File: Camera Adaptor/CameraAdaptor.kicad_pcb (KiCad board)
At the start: 2 copper layers, 6 parts, among them P1 CONN_02X12, P2 CONN_02X09, U1 Oscillator

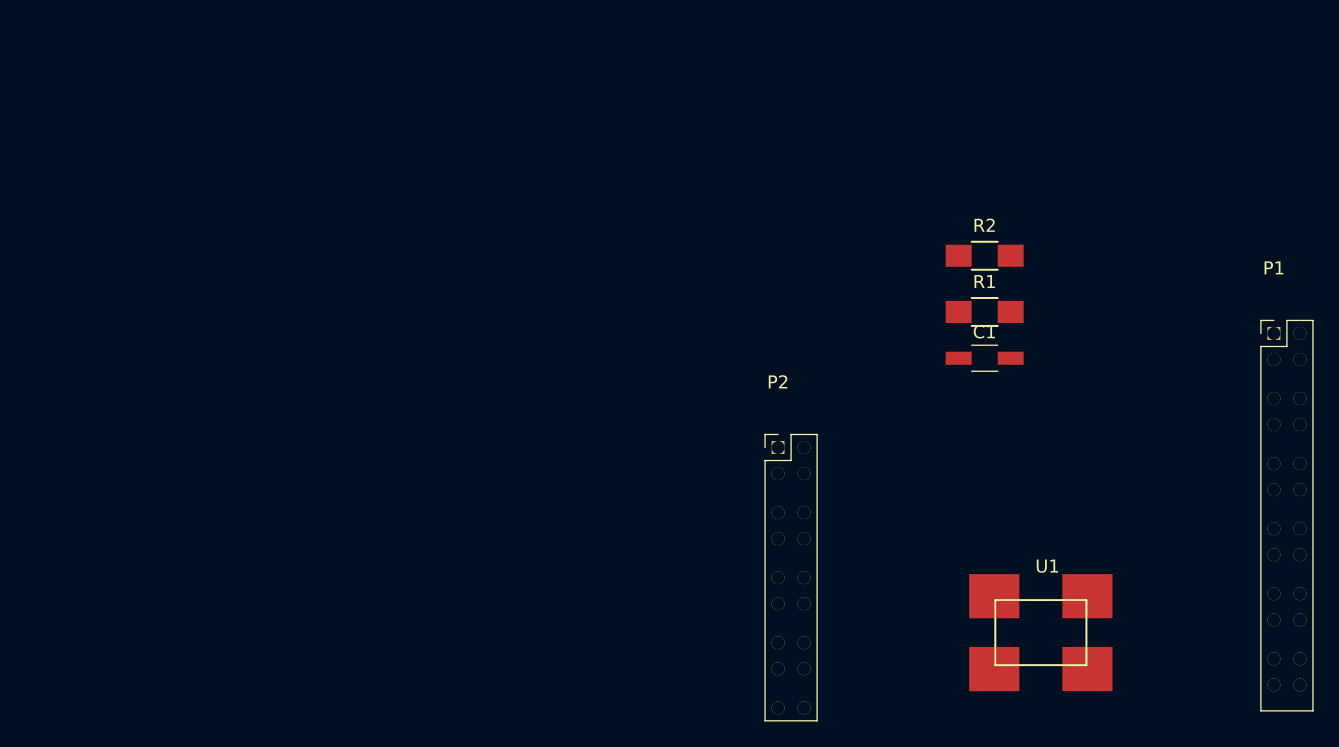
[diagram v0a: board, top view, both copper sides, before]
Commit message: Did the basic layout, avaiting via size, track width specifications.
Signed-off-by: Kolijn Wolfaardt <kolijn.wolfaardt@gmail.com>
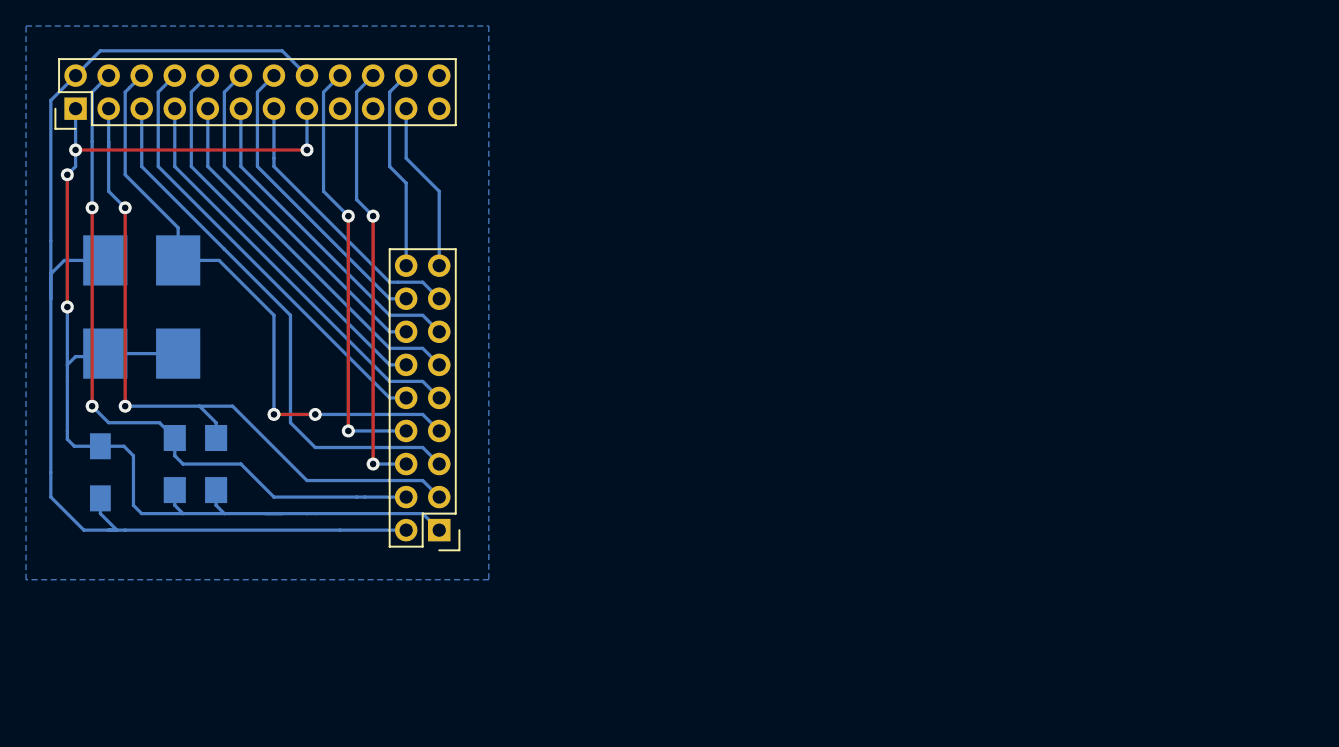
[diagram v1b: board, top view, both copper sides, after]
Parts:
- C1, R1, R2, U1: moved to B.Cu
- moved P1 93.7 mm to (81.9, 81.3), turned to 90 degrees
- moved U1 73.5 mm to (87.0, 96.5), turned to 90 degrees
- moved C1 68.5 mm to (83.8, 109.2), turned to 270 degrees
- moved R2 64.3 mm to (89.5, 108.6), turned to 90 degrees
- moved R1 60.2 mm to (92.7, 108.6), turned to 90 degrees
- moved P2 26.8 mm to (109.9, 113.7), turned to 180 degrees
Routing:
- net +3V3: track 0.00 -> 94.6 mm, vias 0 -> 4
- net GND: track 0.00 -> 91.0 mm
- net /SIOC: track 0.00 -> 54.0 mm, vias 0 -> 2
- net /SIOD: track 0.00 -> 53.7 mm, vias 0 -> 2
- net /PCLK: track 0.00 -> 46.4 mm, vias 0 -> 2
- net /VSync: track 0.00 -> 41.6 mm
- net /D6: track 0.00 -> 33.9 mm
- net /Href: track 0.00 -> 33.4 mm, vias 0 -> 2
- net /XCLK: track 0.00 -> 33.1 mm, vias 0 -> 2
- net /D7: track 0.00 -> 32.1 mm
- net /D4: track 0.00 -> 30.3 mm
- net /D5: track 0.00 -> 28.5 mm
- net /D2: track 0.00 -> 26.7 mm
- net /D3: track 0.00 -> 24.9 mm
- net /D0: track 0.00 -> 23.8 mm
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- added copper zone on B.Cu, net GND
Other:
- net class Default: via_dia 0.6 -> 1; via_drill 0.4 -> 0.8
- rule via_min_drill: 0.3 -> 0.6
- rule via_min_size: 0.4 -> 0.7

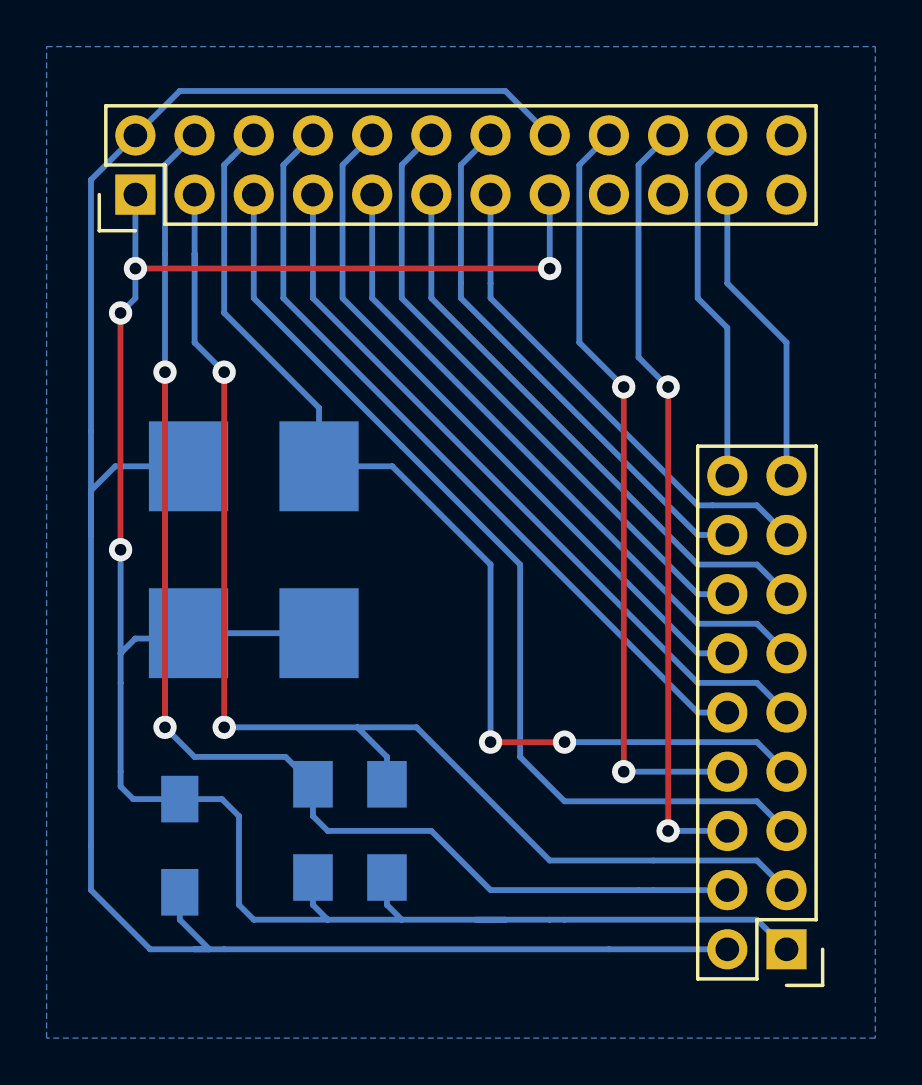
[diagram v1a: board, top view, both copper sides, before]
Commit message: Changed CamerAdaptor layout, changed track thickness
Signed-off-by: Kolijn Wolfaardt <kolijn.wolfaardt@gmail.com>
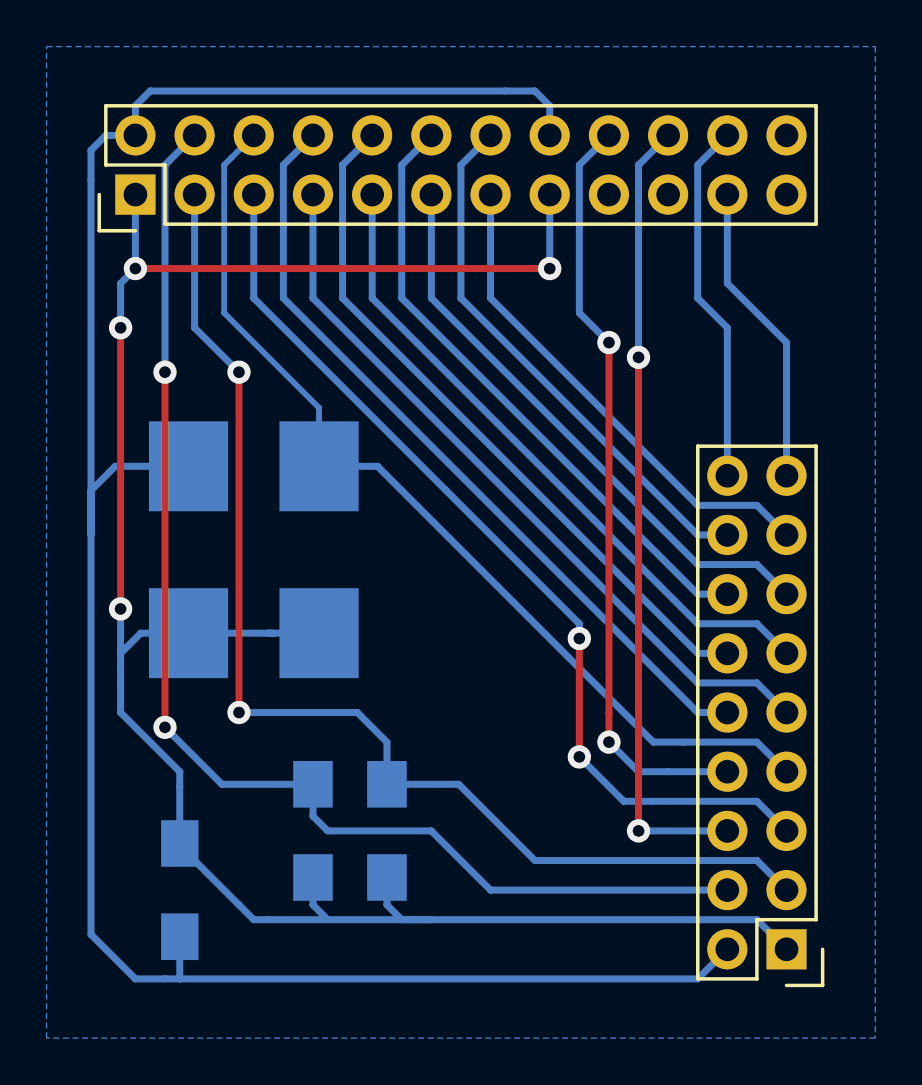
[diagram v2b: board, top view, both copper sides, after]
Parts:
- moved C1 1.91 mm to (83.8, 111.1)
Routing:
- net /PCLK: track 46.4 -> 41.9 mm, vias 2 -> 0
- net /SIOC: track 54.0 -> 50.7 mm
- net GND: track 91.0 -> 93.6 mm
- net /VSync: track 41.6 -> 40.1 mm, vias 0 -> 2
- net /Href: track 33.4 -> 34.2 mm
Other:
- net class Default: trace_width 0.25 -> 0.3
- rule via_min_drill: 0.6 -> 0.7
- rule via_min_size: 0.7 -> 0.8

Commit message: Removed pdf outputs, added correct gerber files
One of the gerber files doesn't register correct with
the cnc machine: The hole should be positioned at 80,100
but ends at 800,100

Signed-off-by: Kolijn Wolfaardt <kolijn.wolfaardt@gmail.com>
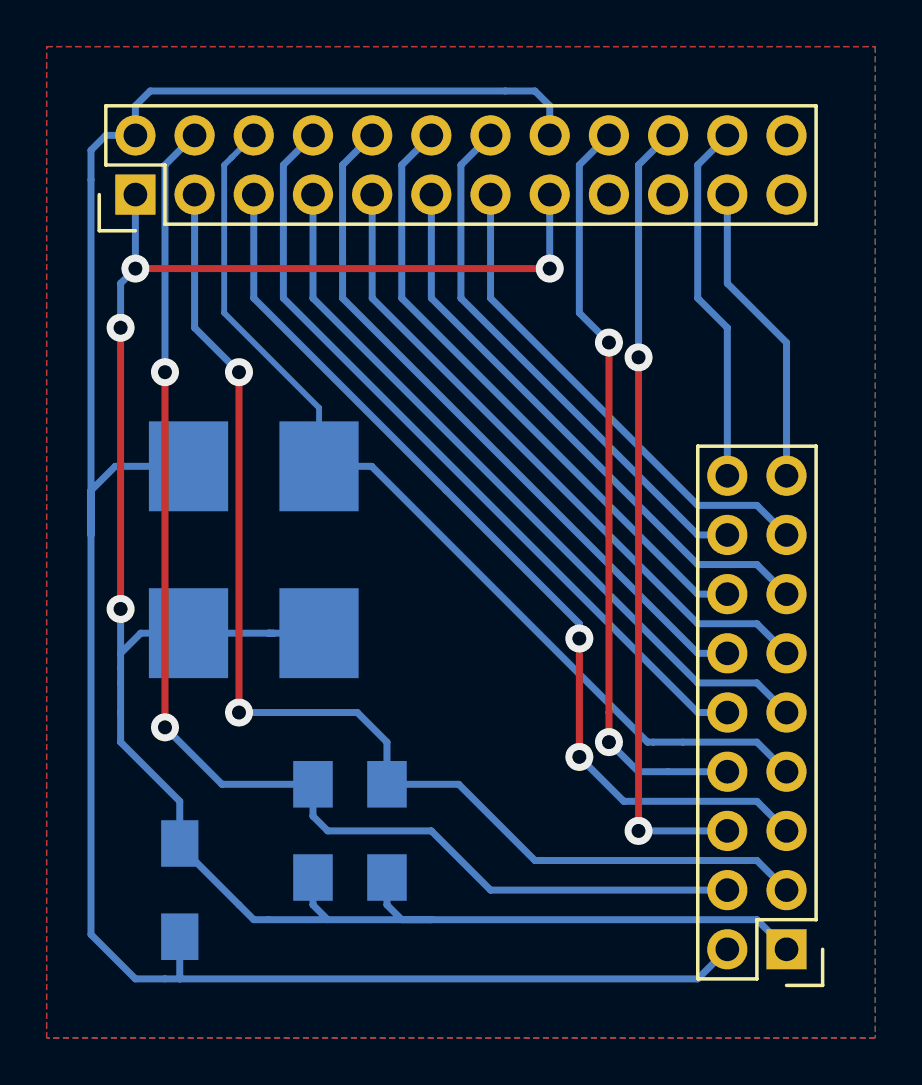
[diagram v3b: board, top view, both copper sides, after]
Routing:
- added copper zone on F.Cu, net GND
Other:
- net class Default: via_dia 1 -> 1.2

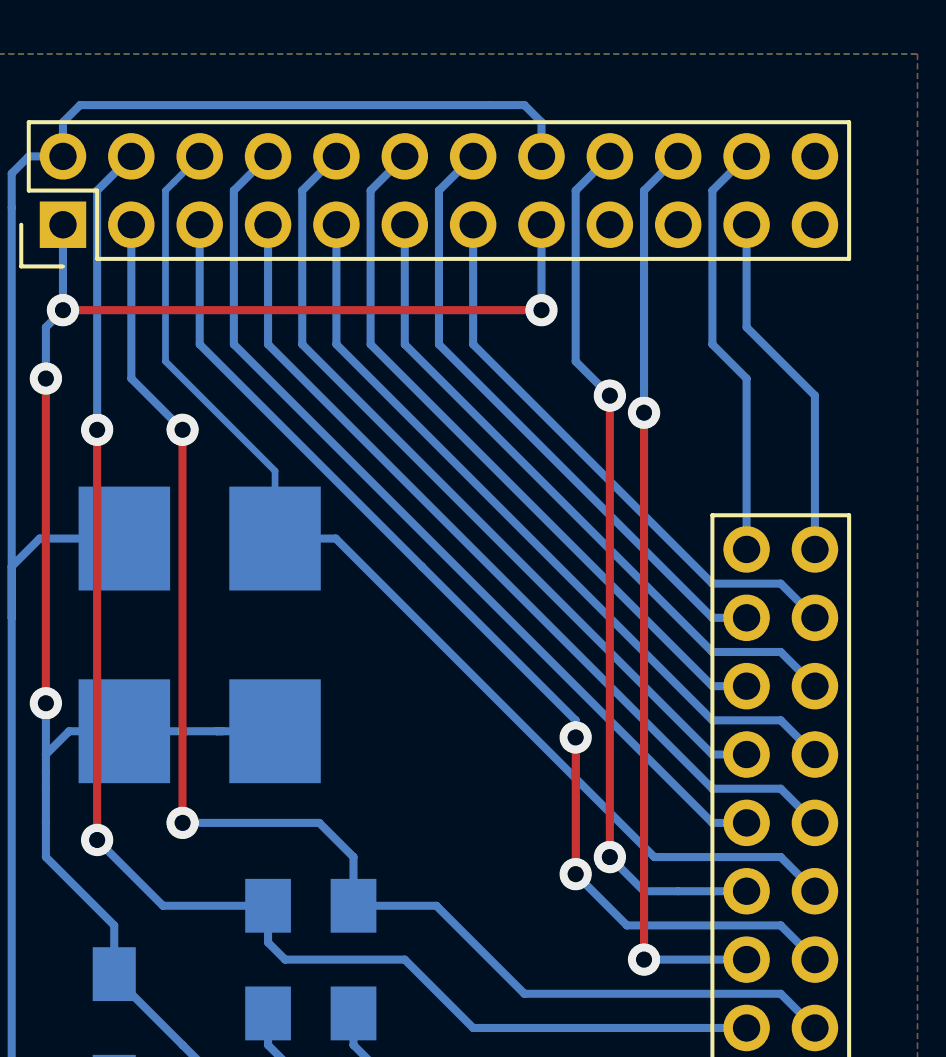
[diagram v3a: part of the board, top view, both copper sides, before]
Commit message: Fixed camera board
Signed-off-by: Kolijn Wolfaardt <kolijn.wolfaardt@gmail.com>
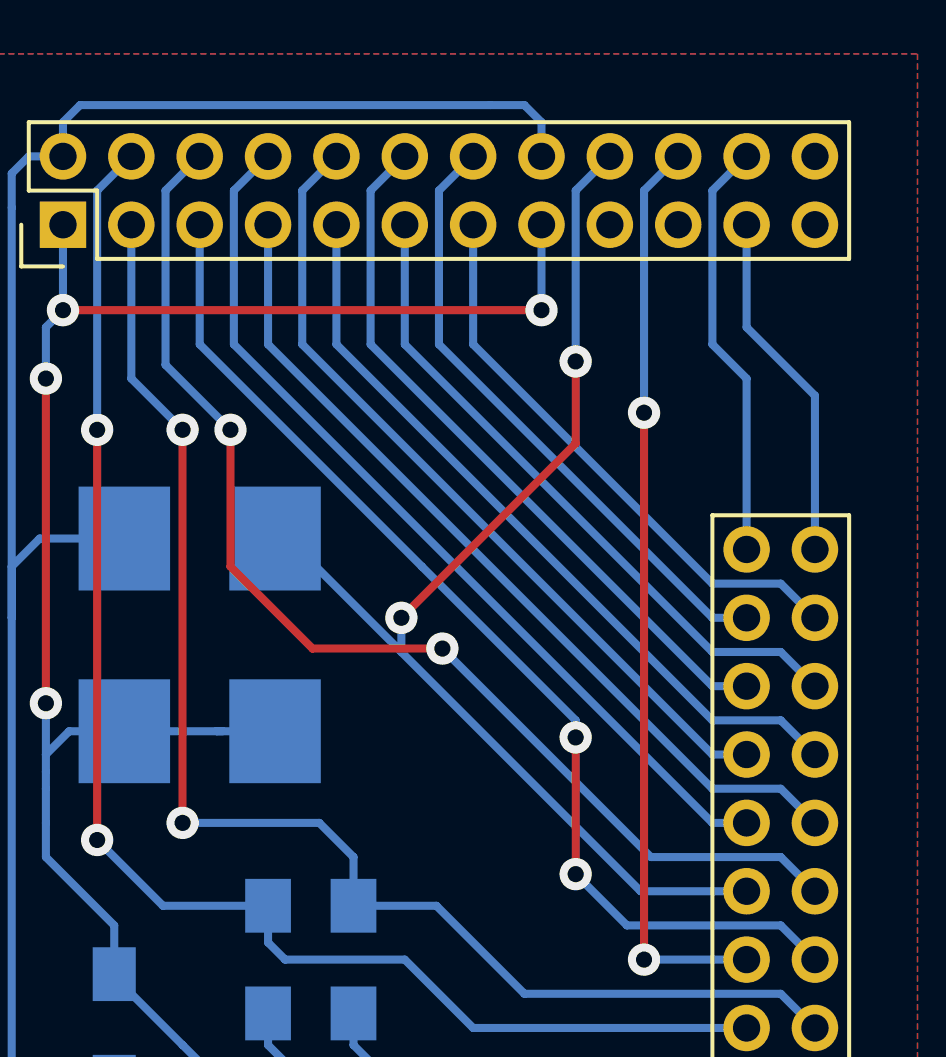
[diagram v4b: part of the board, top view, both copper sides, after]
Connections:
- U1 pad 3: /PCLK -> /XCLK
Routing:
- net /XCLK: track 32.7 -> 44.6 mm
- net /PCLK: track 41.9 -> 43.5 mm, vias 0 -> 2
